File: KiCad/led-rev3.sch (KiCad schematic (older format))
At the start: 83 parts, among them U2 ATTINY88-A

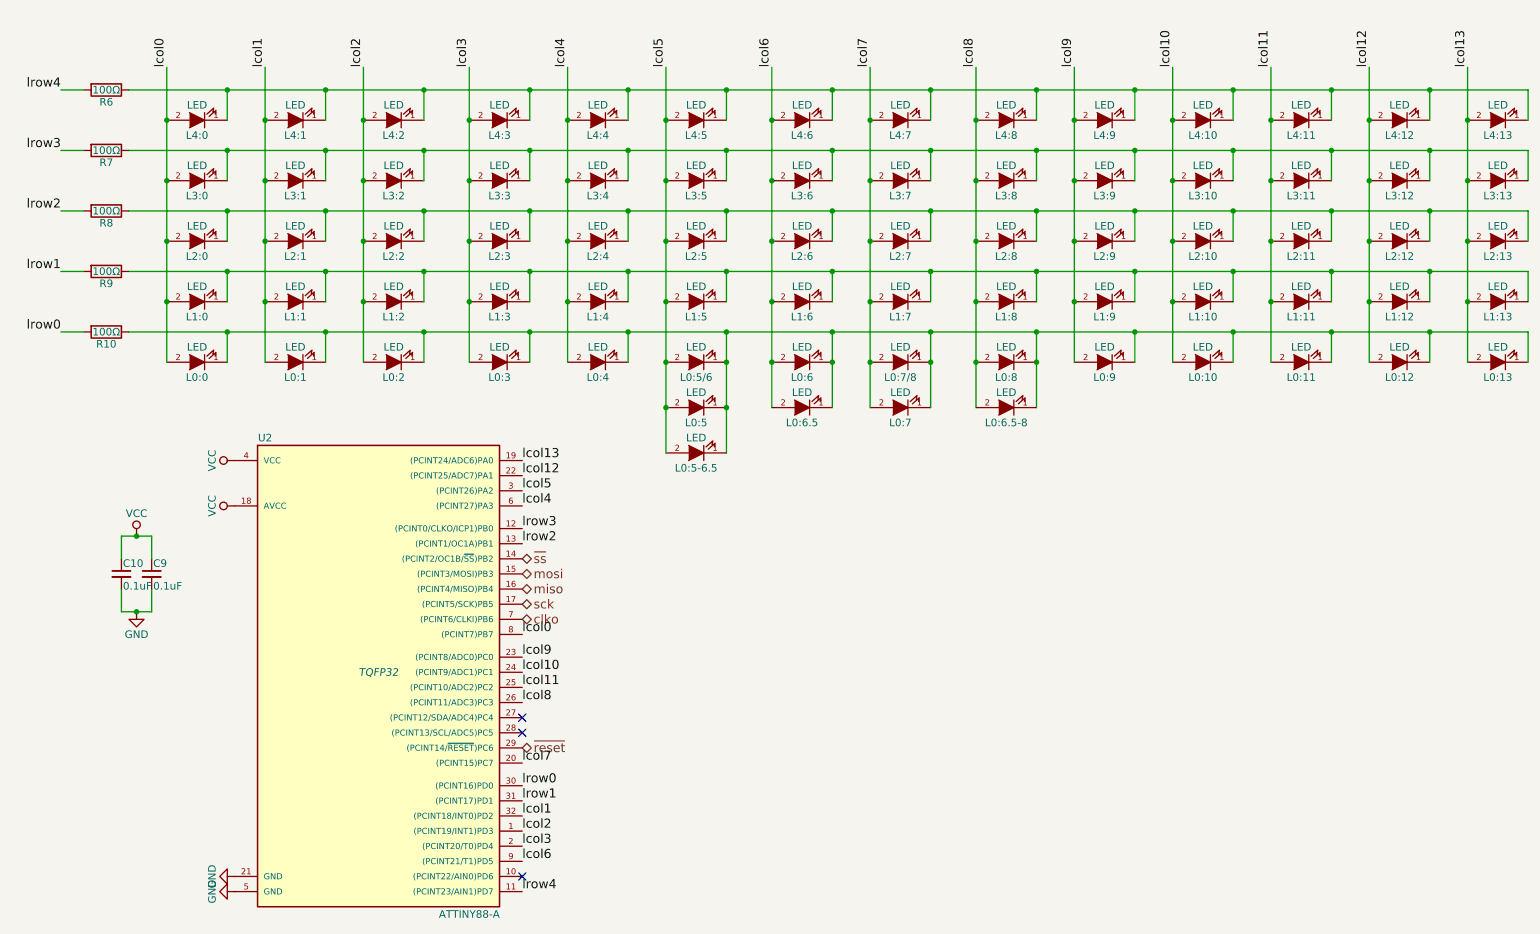
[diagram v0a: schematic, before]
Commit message: adding prototype for revision 3: with more support for other layouts
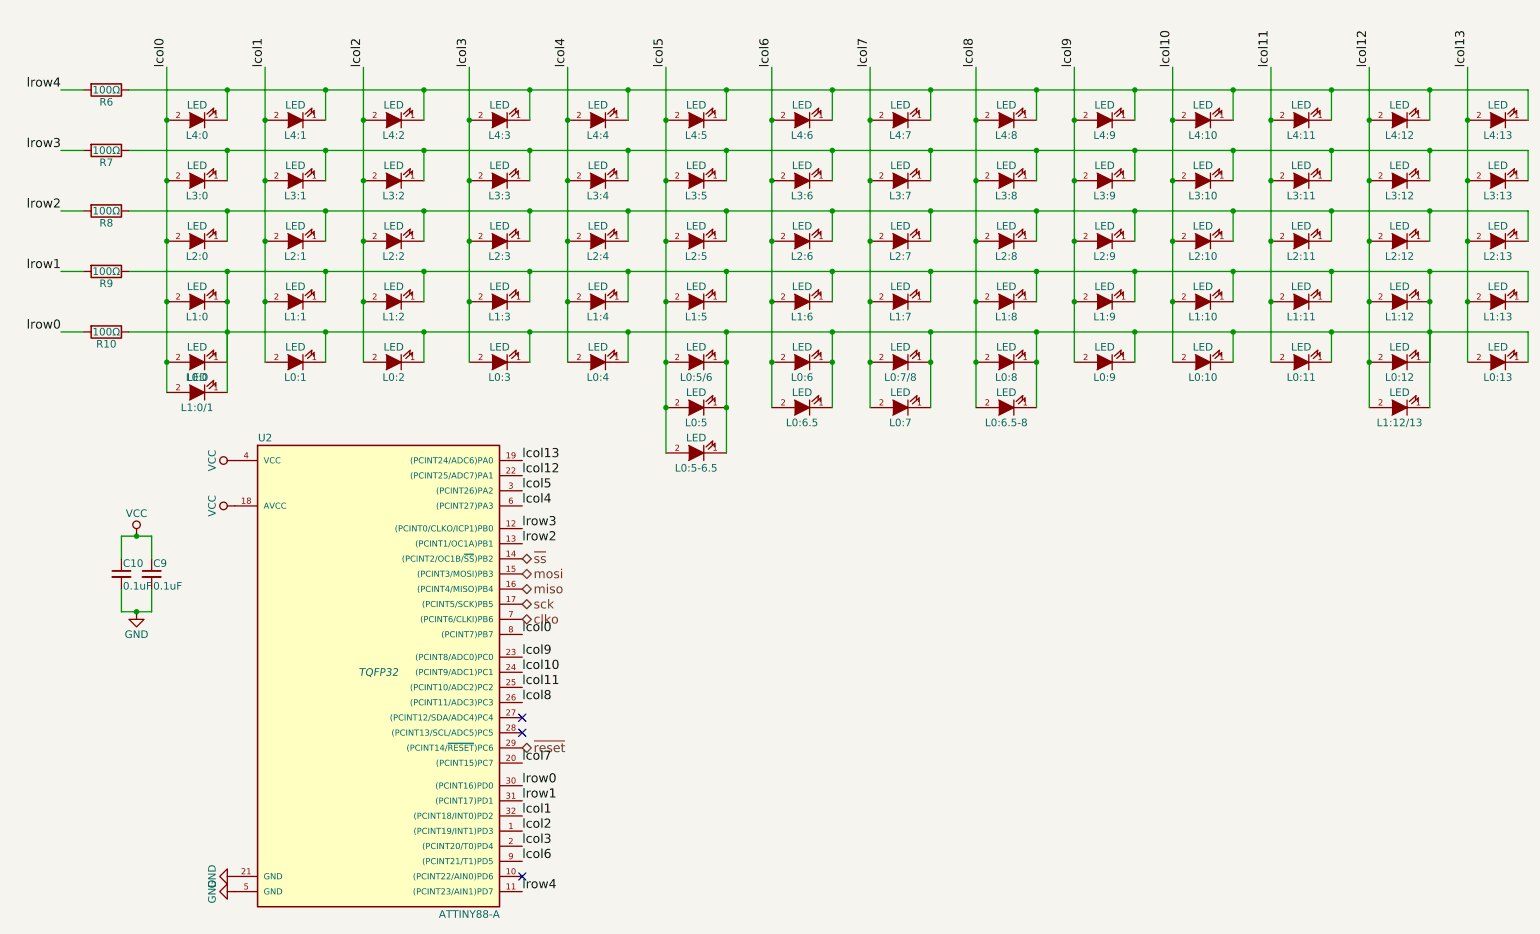
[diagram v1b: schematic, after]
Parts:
- added L1:0/1, L1:12/13: LED, symbol LED
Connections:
- net lcol0: now also L1:0/1.2 (A)
- net lcol12: now also L1:12/13.2 (A)
- net at L0:0.1 (K), L0:1.1 (K), L0:10.1 (K)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: now also L1:0.1 (K), L1:1.1 (K), L1:10.1 (K), L1:11.1 (K), L1:12.1 (K), L1:13.1 (K), L1:2.1 (K), L1:3.1 (K), L1:4.1 (K), L1:5.1 (K), L1:6.1 (K), L1:7.1 (K), L1:8.1 (K), L1:9.1 (K), R9.1, L1:0/1.1 (K), L1:12/13.1 (K)
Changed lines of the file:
@@
 LIBS:components
 LIBS:keyboard-cache
+LIBS:keyboard-rev3-cache
 EELAYER 25 0
 EELAYER END
@@
 	4300 3700 4300 3900
 Wire Wire Line
-	1900 1950 1900 3900
+	1900 1950 1900 4100
 Connection ~ 1900 3100
 Connection ~ 2300 2900
@@
 Connection ~ 2300 3300
 Wire Wire Line
-	2300 3500 2300 3300
+	2300 3300 2300 4100
 Connection ~ 2950 3300
 Wire Wire Line
@@
 Connection ~ 10250 3300
 Wire Wire Line
-	10250 3300 10250 3500
+	10250 3300 10250 4200
 Wire Wire Line
 	10900 3300 10900 3500
@@
 	10250 2100 10250 2300
 Wire Wire Line
-	9850 1950 9850 3900
+	9850 1950 9850 4200
 Wire Wire Line
 	9200 1950 9200 3900
@@
 Wire Wire Line
 	5900 1950 5900 4200
+$Comp
+L LED L1:0/1
+U 1 1 58E2781F
+P 2100 4100
+F 0 "L1:0/1" H 2100 4200 50  0000 C CNN
+F 1 "LED" H 2100 4000 50  0000 C CNN
+F 2 "" H 2100 4100 50  0000 C CNN
+F 3 "" H 2100 4100 50  0000 C CNN
+	1    2100 4100
+	-1   0    0    1
+$EndComp
+Connection ~ 1900 3900
+Connection ~ 2300 3500
+$Comp
+L LED L1:12/13
+U 1 1 58E284DC
+P 10050 4200
+F 0 "L1:12/13" H 10050 4300 50  0000 C CNN
+F 1 "LED" H 10050 4100 50  0000 C CNN
+F 2 "" H 10050 4200 50  0000 C CNN
+F 3 "" H 10050 4200 50  0000 C CNN
+	1    10050 4200
+	-1   0    0    1
+$EndComp
+Connection ~ 9850 3900
+Connection ~ 10250 3500
 $EndSCHEMATC
